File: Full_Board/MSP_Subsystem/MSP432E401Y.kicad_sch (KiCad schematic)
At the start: 4 parts, among them J1-J1 Conn_01x10, J4-J1 Conn_01x10, J5-J1 Conn_01x10, J8-J1 Conn_01x10

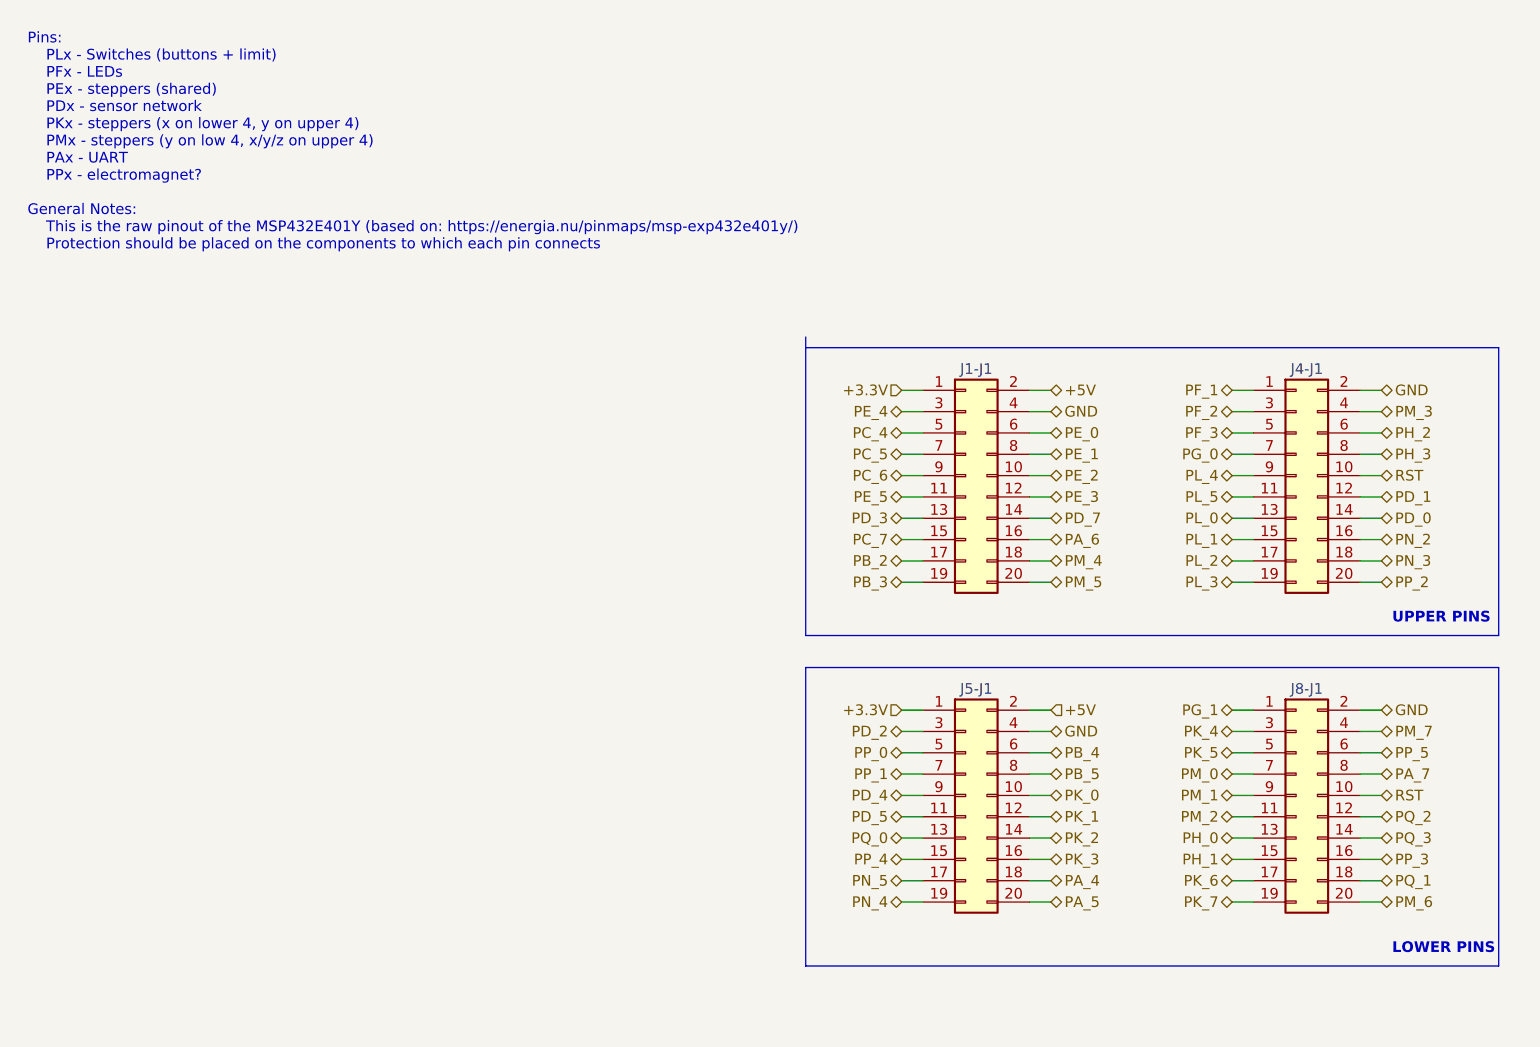
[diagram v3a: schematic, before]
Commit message: Resolve misconfigured components, replace PCB from now completed schematic
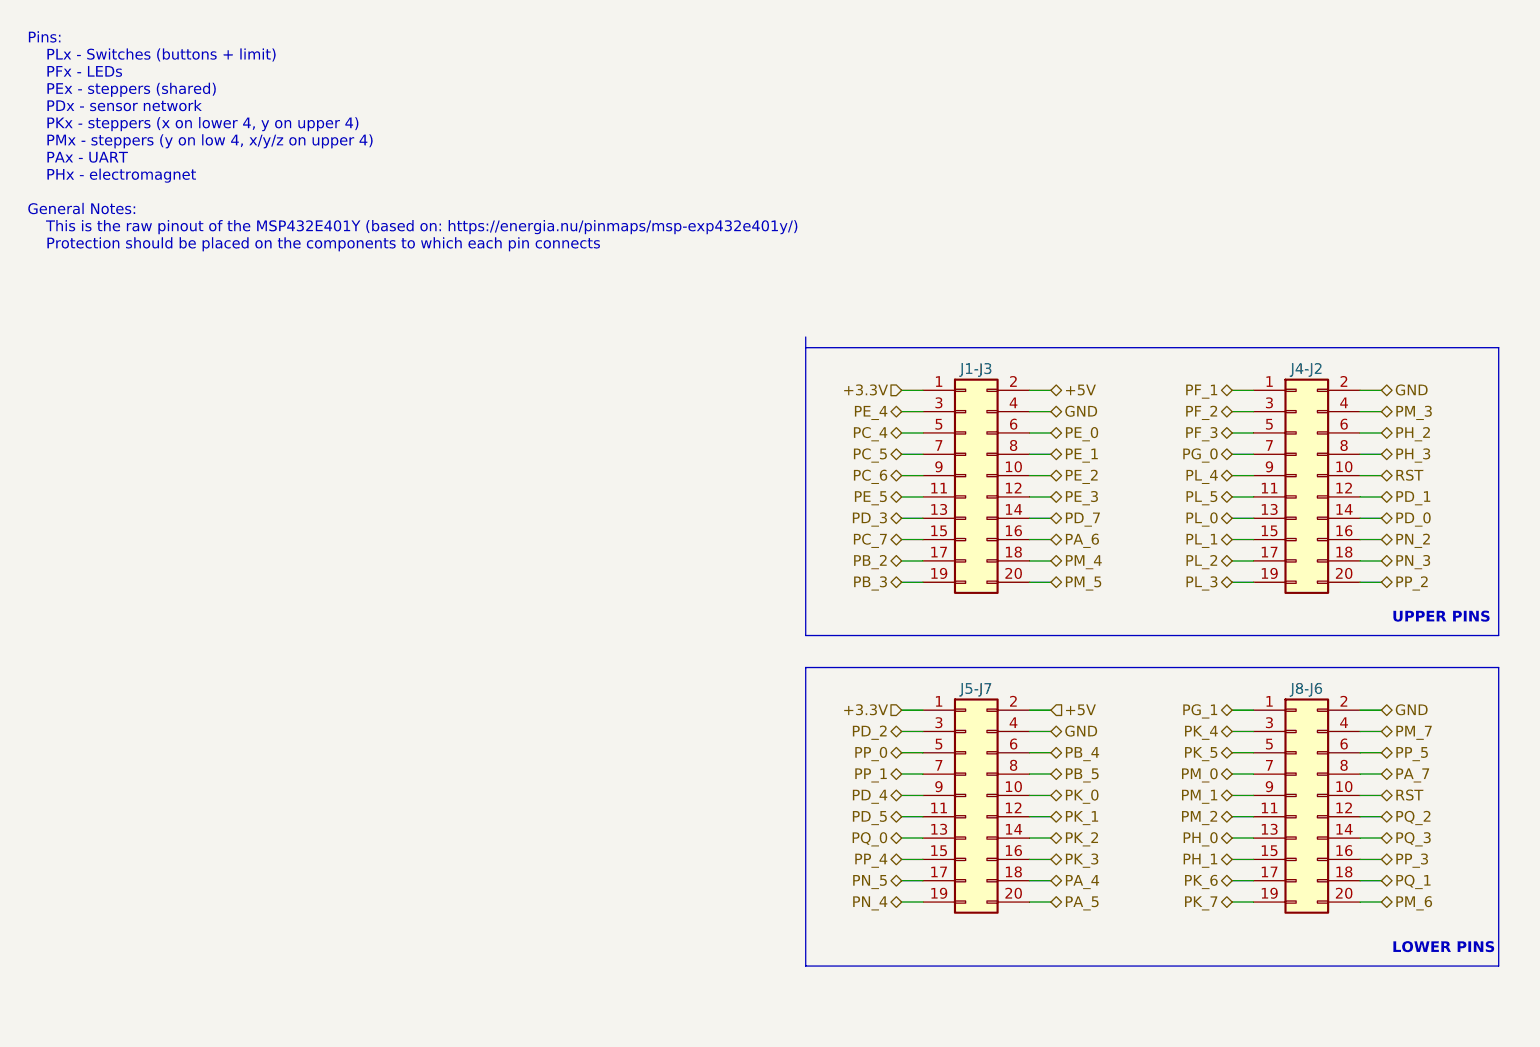
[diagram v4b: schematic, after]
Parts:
- renumbered J1-J1 to J1-J3, J4-J1 to J4-J2, J5-J1 to J5-J7, J8-J1 to J8-J6
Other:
- note added: "Pins: PLx - Switches (buttons + limit) PFx - LEDs PEx - steppers (shared) PDx - sensor network PKx - steppers (x on lower 4, y on upper 4) PMx - steppers (y on low 4, x/y/z on upper 4) PAx - UART PHx - electromagnet General Notes: This is the raw pinout of the MSP432E401Y (based on: https://energia.nu/pinmaps/msp-exp432e401y/) Protection should be placed on the components to which each pin connec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"
- note removed: "Pins: PLx - Switches (buttons + limit) PFx - LEDs PEx - steppers (shared) PDx - sensor network PKx - steppers (x on lower 4, y on upper 4) PMx - steppers (y on low 4, x/y/z on upper 4) PAx - UART PPx - electromagnet? General Notes: This is the raw pinout of the MSP432E401Y (based on: https://energia.nu/pinmaps/msp-exp432e401y/) Protection should be placed on the components to which each pin conne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"
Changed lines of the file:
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@@
     (stroke (width 0) (type default) (color 0 0 0 0))
   )
-  (text "Pins:\n	PLx - Switches (buttons + limit)\n	PFx - LEDs\n	PEx - steppers (shared)\n	PDx - sensor network\n	PKx - steppers (x on lower 4, y on upper 4)\n	PMx - steppers (y on low 4, x/y/z on upper 4)\n	PAx - UART\n	PPx - electromagnet?\n\nGeneral Notes:\n	This is the raw pinout of the MSP432E401Y (based on: https://energia.nu/pinmaps/msp-exp432e401y/)\n	Protection should be placed on the components to which each pin connects"
+  (text "Pins:\n	PLx - Switches (buttons + limit)\n	PFx - LEDs\n	PEx - steppers (shared)\n	PDx - sensor network\n	PKx - steppers (x on lower 4, y on upper 4)\n	PMx - steppers (y on low 4, x/y/z on upper 4)\n	PAx - UART\n	PHx - electromagnet\n\nGeneral Notes:\n	This is the raw pinout of the MSP432E401Y (based on: https://energia.nu/pinmaps/msp-exp432e401y/)\n	Protection should be placed on the components to which each pin connects"
     (at 16.51 44.45 0)
     (effects (font (size 1.27 1.27)) (justify left bottom))
@@
   (symbol (lib_id "Connector_Generic:Conn_02x10_Odd_Even") (at 167.64 71.12 0) (unit 1)
     (in_bom yes) (on_board yes)
-    (property "Reference" "J4-J1" (id 0) (at 168.91 58.42 0))
+    (property "Reference" "J4-J2" (id 0) (at 168.91 58.42 0))
     (property "Value" "Conn_01x10" (id 1) (at 165.1 87.63 0)
       (effects (font (size 1.27 1.27)) hide)
@@
   (symbol (lib_id "Connector_Generic:Conn_02x10_Odd_Even") (at 128.27 109.22 0) (unit 1)
     (in_bom yes) (on_board yes)
-    (property "Reference" "J5-J1" (id 0) (at 129.54 96.52 0))
+    (property "Reference" "J5-J7" (id 0) (at 129.54 96.52 0))
     (property "Value" "Conn_01x10" (id 1) (at 130.81 113.03 0)
       (effects (font (size 1.27 1.27)) (justify left) hide)
@@
   (symbol (lib_id "Connector_Generic:Conn_02x10_Odd_Even") (at 167.64 109.22 0) (unit 1)
     (in_bom yes) (on_board yes)
-    (property "Reference" "J8-J1" (id 0) (at 168.91 96.52 0))
+    (property "Reference" "J8-J6" (id 0) (at 168.91 96.52 0))
     (property "Value" "Conn_01x10" (id 1) (at 165.1 125.73 0)
       (effects (font (size 1.27 1.27)) hide)
@@
   (symbol (lib_id "Connector_Generic:Conn_02x10_Odd_Even") (at 128.27 71.12 0) (unit 1)
     (in_bom yes) (on_board yes)
-    (property "Reference" "J1-J1" (id 0) (at 129.54 58.42 0))
+    (property "Reference" "J1-J3" (id 0) (at 129.54 58.42 0))
     (property "Value" "Conn_01x10" (id 1) (at 130.81 74.93 0)
       (effects (font (size 1.27 1.27)) (justify left) hide)

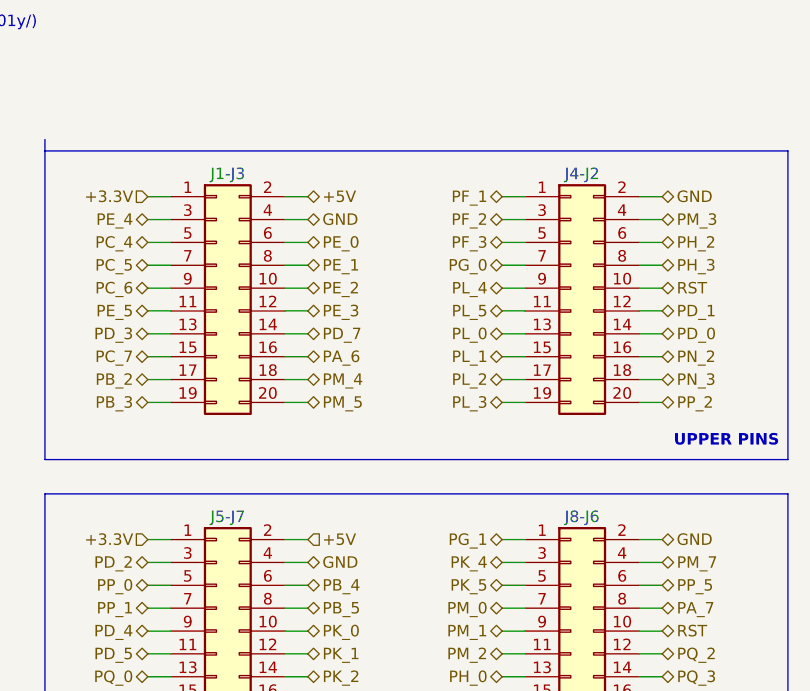
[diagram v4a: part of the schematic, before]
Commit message: Redo pinout, finish pcb layout (no traces)
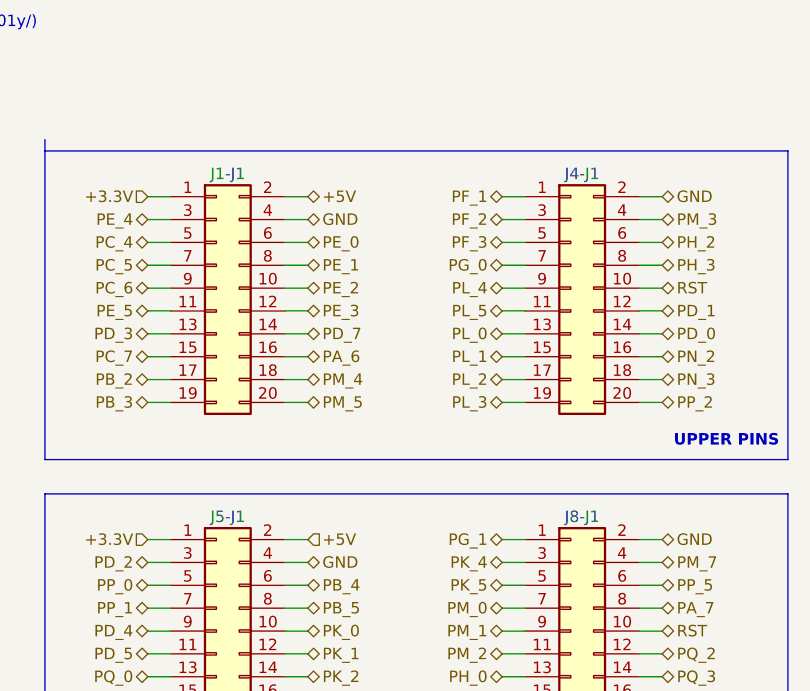
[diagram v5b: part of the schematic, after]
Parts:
- renumbered J1-J3 to J1-J1, J4-J2 to J4-J1, J5-J7 to J5-J1, J8-J6 to J8-J1
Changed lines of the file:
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@@
   (symbol (lib_id "Connector_Generic:Conn_02x10_Odd_Even") (at 167.64 71.12 0) (unit 1)
     (in_bom yes) (on_board yes)
-    (property "Reference" "J4-J2" (id 0) (at 168.91 58.42 0))
+    (property "Reference" "J4-J1" (id 0) (at 168.91 58.42 0))
     (property "Value" "Conn_01x10" (id 1) (at 165.1 87.63 0)
       (effects (font (size 1.27 1.27)) hide)
@@
   (symbol (lib_id "Connector_Generic:Conn_02x10_Odd_Even") (at 128.27 109.22 0) (unit 1)
     (in_bom yes) (on_board yes)
-    (property "Reference" "J5-J7" (id 0) (at 129.54 96.52 0))
+    (property "Reference" "J5-J1" (id 0) (at 129.54 96.52 0))
     (property "Value" "Conn_01x10" (id 1) (at 130.81 113.03 0)
       (effects (font (size 1.27 1.27)) (justify left) hide)
@@
   (symbol (lib_id "Connector_Generic:Conn_02x10_Odd_Even") (at 167.64 109.22 0) (unit 1)
     (in_bom yes) (on_board yes)
-    (property "Reference" "J8-J6" (id 0) (at 168.91 96.52 0))
+    (property "Reference" "J8-J1" (id 0) (at 168.91 96.52 0))
     (property "Value" "Conn_01x10" (id 1) (at 165.1 125.73 0)
       (effects (font (size 1.27 1.27)) hide)
@@
   (symbol (lib_id "Connector_Generic:Conn_02x10_Odd_Even") (at 128.27 71.12 0) (unit 1)
     (in_bom yes) (on_board yes)
-    (property "Reference" "J1-J3" (id 0) (at 129.54 58.42 0))
+    (property "Reference" "J1-J1" (id 0) (at 129.54 58.42 0))
     (property "Value" "Conn_01x10" (id 1) (at 130.81 74.93 0)
       (effects (font (size 1.27 1.27)) (justify left) hide)

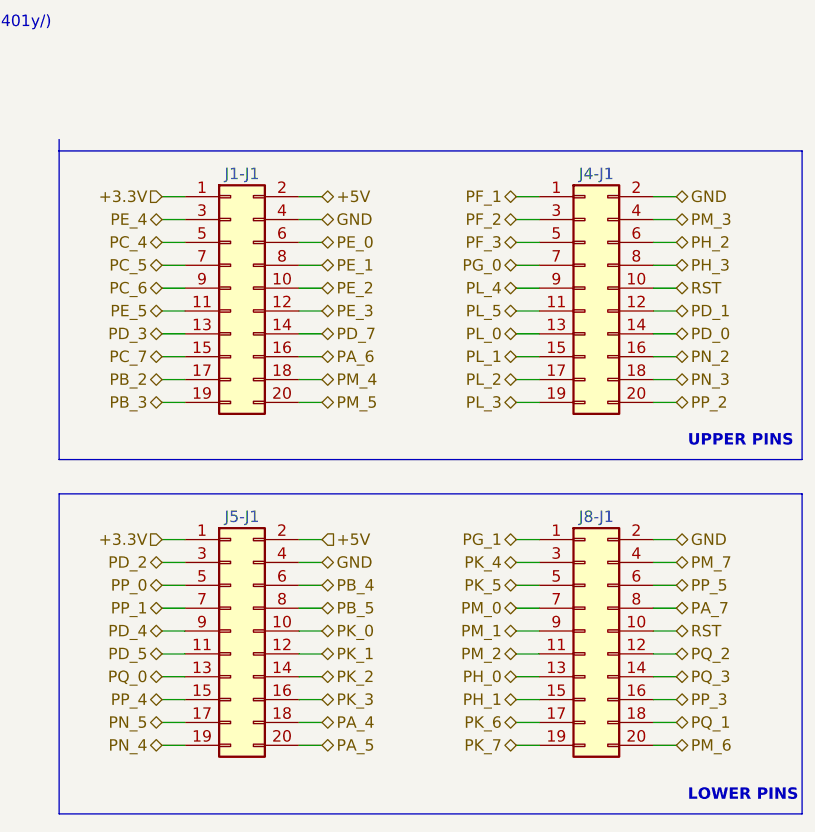
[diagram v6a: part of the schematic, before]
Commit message: Flipped the MSP headers
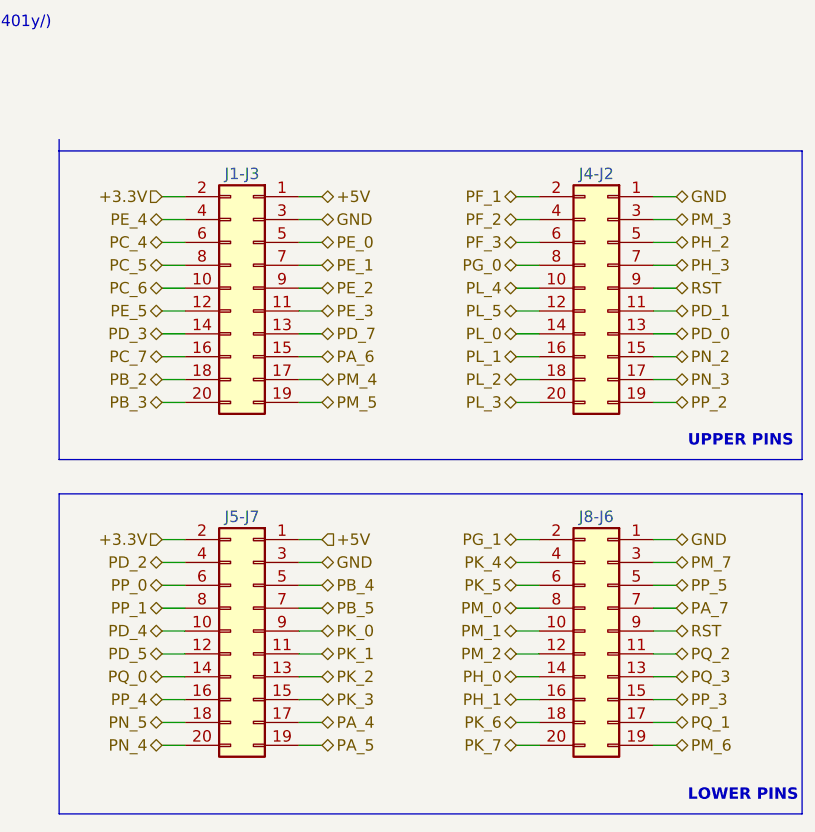
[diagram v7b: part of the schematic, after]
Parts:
- renumbered J1-J1 to J1-J3, J4-J1 to J4-J2, J5-J1 to J5-J7, J8-J1 to J8-J6
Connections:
- net +3.3V: now also J1-J3.2 (Pin_2), J5-J7.2 (Pin_2); no longer J1-J3.1 (Pin_1), J5-J7.1 (Pin_1)
- net +5V: now also J1-J3.1 (Pin_1), J5-J7.1 (Pin_1); no longer J1-J3.2 (Pin_2), J5-J7.2 (Pin_2)
- net GND: now also J1-J3.3 (Pin_3), J4-J2.1 (Pin_1), J5-J7.3 (Pin_3), J8-J6.1 (Pin_1); no longer J1-J3.4 (Pin_4), J4-J2.2 (Pin_2), J5-J7.4 (Pin_4), J8-J6.2 (Pin_2)
- net PA_4: now also J5-J7.17 (Pin_17); no longer J5-J7.18 (Pin_18)
- net PA_5: now also J5-J7.19 (Pin_19); no longer J5-J7.20 (Pin_20)
- net PA_6: now also J1-J3.15 (Pin_15); no longer J1-J3.16 (Pin_16)
- net PA_7: now also J8-J6.7 (Pin_7); no longer J8-J6.8 (Pin_8)
- net PB_2: now also J1-J3.18 (Pin_18); no longer J1-J3.17 (Pin_17)
- net PB_3: now also J1-J3.20 (Pin_20); no longer J1-J3.19 (Pin_19)
- net PB_4: now also J5-J7.5 (Pin_5); no longer J5-J7.6 (Pin_6)
- net PB_5: now also J5-J7.7 (Pin_7); no longer J5-J7.8 (Pin_8)
- net PC_4: now also J1-J3.6 (Pin_6); no longer J1-J3.5 (Pin_5)
- net PC_5: now also J1-J3.8 (Pin_8); no longer J1-J3.7 (Pin_7)
- net PC_6: now also J1-J3.10 (Pin_10); no longer J1-J3.9 (Pin_9)
- net PC_7: now also J1-J3.16 (Pin_16); no longer J1-J3.15 (Pin_15)
- net PD_0: now also J4-J2.13 (Pin_13); no longer J4-J2.14 (Pin_14)
- net PD_1: now also J4-J2.11 (Pin_11); no longer J4-J2.12 (Pin_12)
- net PD_2: now also J5-J7.4 (Pin_4); no longer J5-J7.3 (Pin_3)
- net PD_3: now also J1-J3.14 (Pin_14); no longer J1-J3.13 (Pin_13)
- net PD_4: now also J5-J7.10 (Pin_10); no longer J5-J7.9 (Pin_9)
- net PD_5: now also J5-J7.12 (Pin_12); no longer J5-J7.11 (Pin_11)
- net PD_7: now also J1-J3.13 (Pin_13); no longer J1-J3.14 (Pin_14)
- net PE_0: now also J1-J3.5 (Pin_5); no longer J1-J3.6 (Pin_6)
- net PE_1: now also J1-J3.7 (Pin_7); no longer J1-J3.8 (Pin_8)
- net PE_2: now also J1-J3.9 (Pin_9); no longer J1-J3.10 (Pin_10)
- net PE_3: now also J1-J3.11 (Pin_11); no longer J1-J3.12 (Pin_12)
- net PE_4: now also J1-J3.4 (Pin_4); no longer J1-J3.3 (Pin_3)
- net PE_5: now also J1-J3.12 (Pin_12); no longer J1-J3.11 (Pin_11)
- net PF_1: now also J4-J2.2 (Pin_2); no longer J4-J2.1 (Pin_1)
- net PF_2: now also J4-J2.4 (Pin_4); no longer J4-J2.3 (Pin_3)
- net PF_3: now also J4-J2.6 (Pin_6); no longer J4-J2.5 (Pin_5)
- net PG_0: now also J4-J2.8 (Pin_8); no longer J4-J2.7 (Pin_7)
- net PG_1: now also J8-J6.2 (Pin_2); no longer J8-J6.1 (Pin_1)
- net PH_0: now also J8-J6.14 (Pin_14); no longer J8-J6.13 (Pin_13)
- net PH_1: now also J8-J6.16 (Pin_16); no longer J8-J6.15 (Pin_15)
- net PH_2: now also J4-J2.5 (Pin_5); no longer J4-J2.6 (Pin_6)
- net PH_3: now also J4-J2.7 (Pin_7); no longer J4-J2.8 (Pin_8)
- net PK_0: now also J5-J7.9 (Pin_9); no longer J5-J7.10 (Pin_10)
- net PK_1: now also J5-J7.11 (Pin_11); no longer J5-J7.12 (Pin_12)
- net PK_2: now also J5-J7.13 (Pin_13); no longer J5-J7.14 (Pin_14)
- net PK_3: now also J5-J7.15 (Pin_15); no longer J5-J7.16 (Pin_16)
- net PK_4: now also J8-J6.4 (Pin_4); no longer J8-J6.3 (Pin_3)
- net PK_5: now also J8-J6.6 (Pin_6); no longer J8-J6.5 (Pin_5)
- net PK_6: now also J8-J6.18 (Pin_18); no longer J8-J6.17 (Pin_17)
- net PK_7: now also J8-J6.20 (Pin_20); no longer J8-J6.19 (Pin_19)
- net PL_0: now also J4-J2.14 (Pin_14); no longer J4-J2.13 (Pin_13)
- net PL_1: now also J4-J2.16 (Pin_16); no longer J4-J2.15 (Pin_15)
- net PL_2: now also J4-J2.18 (Pin_18); no longer J4-J2.17 (Pin_17)
- net PL_3: now also J4-J2.20 (Pin_20); no longer J4-J2.19 (Pin_19)
- net PL_4: now also J4-J2.10 (Pin_10); no longer J4-J2.9 (Pin_9)
- net PL_5: now also J4-J2.12 (Pin_12); no longer J4-J2.11 (Pin_11)
- net PM_0: now also J8-J6.8 (Pin_8); no longer J8-J6.7 (Pin_7)
- net PM_1: now also J8-J6.10 (Pin_10); no longer J8-J6.9 (Pin_9)
- net PM_2: now also J8-J6.12 (Pin_12); no longer J8-J6.11 (Pin_11)
- net PM_3: now also J4-J2.3 (Pin_3); no longer J4-J2.4 (Pin_4)
- net PM_4: now also J1-J3.17 (Pin_17); no longer J1-J3.18 (Pin_18)
- net PM_5: now also J1-J3.19 (Pin_19); no longer J1-J3.20 (Pin_20)
- net PM_6: now also J8-J6.19 (Pin_19); no longer J8-J6.20 (Pin_20)
- net PM_7: now also J8-J6.3 (Pin_3); no longer J8-J6.4 (Pin_4)
- net PN_2: now also J4-J2.15 (Pin_15); no longer J4-J2.16 (Pin_16)
- net PN_3: now also J4-J2.17 (Pin_17); no longer J4-J2.18 (Pin_18)
- net PN_4: now also J5-J7.20 (Pin_20); no longer J5-J7.19 (Pin_19)
- net PN_5: now also J5-J7.18 (Pin_18); no longer J5-J7.17 (Pin_17)
- net PP_0: now also J5-J7.6 (Pin_6); no longer J5-J7.5 (Pin_5)
- net PP_1: now also J5-J7.8 (Pin_8); no longer J5-J7.7 (Pin_7)
- net PP_2: now also J4-J2.19 (Pin_19); no longer J4-J2.20 (Pin_20)
- net PP_3: now also J8-J6.15 (Pin_15); no longer J8-J6.16 (Pin_16)
- net PP_4: now also J5-J7.16 (Pin_16); no longer J5-J7.15 (Pin_15)
- net PP_5: now also J8-J6.5 (Pin_5); no longer J8-J6.6 (Pin_6)
- net PQ_0: now also J5-J7.14 (Pin_14); no longer J5-J7.13 (Pin_13)
- net PQ_1: now also J8-J6.17 (Pin_17); no longer J8-J6.18 (Pin_18)
- net PQ_2: now also J8-J6.11 (Pin_11); no longer J8-J6.12 (Pin_12)
- net PQ_3: now also J8-J6.13 (Pin_13); no longer J8-J6.14 (Pin_14)
- net RST: now also J4-J2.9 (Pin_9), J8-J6.9 (Pin_9); no longer J4-J2.10 (Pin_10), J8-J6.10 (Pin_10)
